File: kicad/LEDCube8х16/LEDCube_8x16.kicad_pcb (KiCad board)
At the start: 2 copper layers, 60 parts, among them J1 USB_OTG, J10 6, J11 7, J12 8, J13 RX, J14 TX, J3 1, J4 2, J5 3, J6 vert layers, J7 ICSP, J8 4, J9 5, Q1 BCP 51.115, Q10 BCP 51.115, Q11 BCP 51.115, Q12 BCP 51.115, Q13 BCP 51.115, Q14 BCP 51.115, Q15 BCP 51.115, Q16 BCP 51.115, Q2 BCP 51.115, Q3 BCP 51.115, Q4 BCP 51.115, Q5 BCP 51.115, Q6 BCP 51.115, Q7 BCP 51.115, Q8 BCP 51.115, Q9 BCP 51.115, U1 ATMEGA644P, U2 TSOP312xx, Y1 16mhz

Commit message: fixes in scheme
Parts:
- added C4: 4400 mkf x 6.3 v, Capacitors_THT:CP_Radial_D18.0mm_P7.50mm, F.Cu at (93.8, 136.5)
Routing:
- net Net-(J1-Pad6): track 13.6 -> 28.9 mm
- net Net-(C4-Pad1): track 301.2 -> 311.0 mm
- net GND: track 150.2 -> 157.2 mm

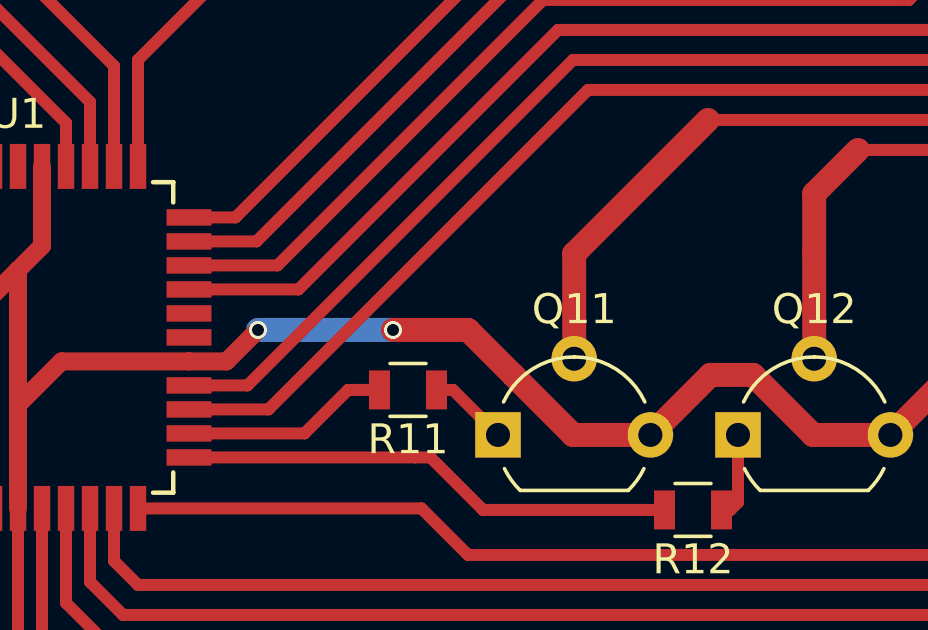
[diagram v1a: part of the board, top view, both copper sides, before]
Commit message: added resistor between mcu and leds
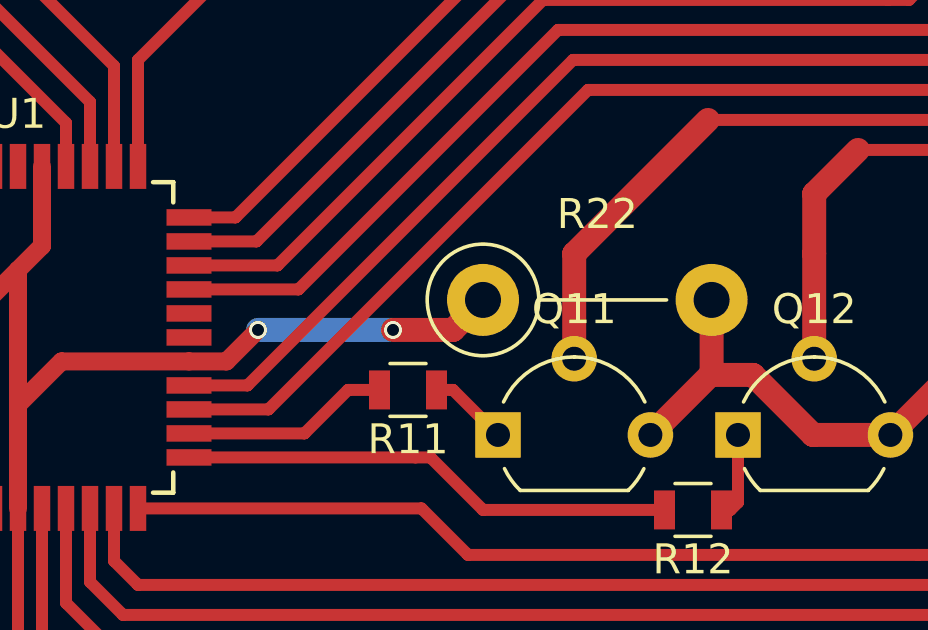
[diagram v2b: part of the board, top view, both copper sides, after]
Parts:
- added R22: 4R, Resistors_THT:R_Axial_DIN0411_L9.9mm_D3.6mm_P7.62mm_Vertical, F.Cu at (118.0, 115.5)
- R1, R3, R4, R5: value R -> 1k
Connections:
- MB1 pad 24: Net-(C4-Pad1) -> Net-(MB1-Pad24)
- MB2 pad 24: Net-(C4-Pad1) -> Net-(MB1-Pad24)
- MB3 pad 24: Net-(C4-Pad1) -> Net-(MB1-Pad24)
- MB4 pad 24: Net-(C4-Pad1) -> Net-(MB1-Pad24)
- Q1 pad 3: Net-(C4-Pad1) -> Net-(MB1-Pad24)
- Q10 pad 3: Net-(C4-Pad1) -> Net-(MB1-Pad24)
- Q11 pad 3: Net-(C4-Pad1) -> Net-(MB1-Pad24)
- Q12 pad 3: Net-(C4-Pad1) -> Net-(MB1-Pad24)
- Q13 pad 3: Net-(C4-Pad1) -> Net-(MB1-Pad24)
- Q14 pad 3: Net-(C4-Pad1) -> Net-(MB1-Pad24)
- Q15 pad 3: Net-(C4-Pad1) -> Net-(MB1-Pad24)
- Q16 pad 3: Net-(C4-Pad1) -> Net-(MB1-Pad24)
- Q2 pad 3: Net-(C4-Pad1) -> Net-(MB1-Pad24)
- Q3 pad 3: Net-(C4-Pad1) -> Net-(MB1-Pad24)
- Q4 pad 3: Net-(C4-Pad1) -> Net-(MB1-Pad24)
- Q5 pad 3: Net-(C4-Pad1) -> Net-(MB1-Pad24)
- Q6 pad 3: Net-(C4-Pad1) -> Net-(MB1-Pad24)
- Q7 pad 3: Net-(C4-Pad1) -> Net-(MB1-Pad24)
- Q8 pad 3: Net-(C4-Pad1) -> Net-(MB1-Pad24)
- Q9 pad 3: Net-(C4-Pad1) -> Net-(MB1-Pad24)
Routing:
- net Net-(C4-Pad1): track 311.0 -> 88.3 mm, vias 6 -> 4
- net Net-(MB1-Pad24): track 0.00 -> 218.7 mm, vias 0 -> 2
